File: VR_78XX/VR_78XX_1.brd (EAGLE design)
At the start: 80 x 100 mm, 28 parts, among them U1 7809

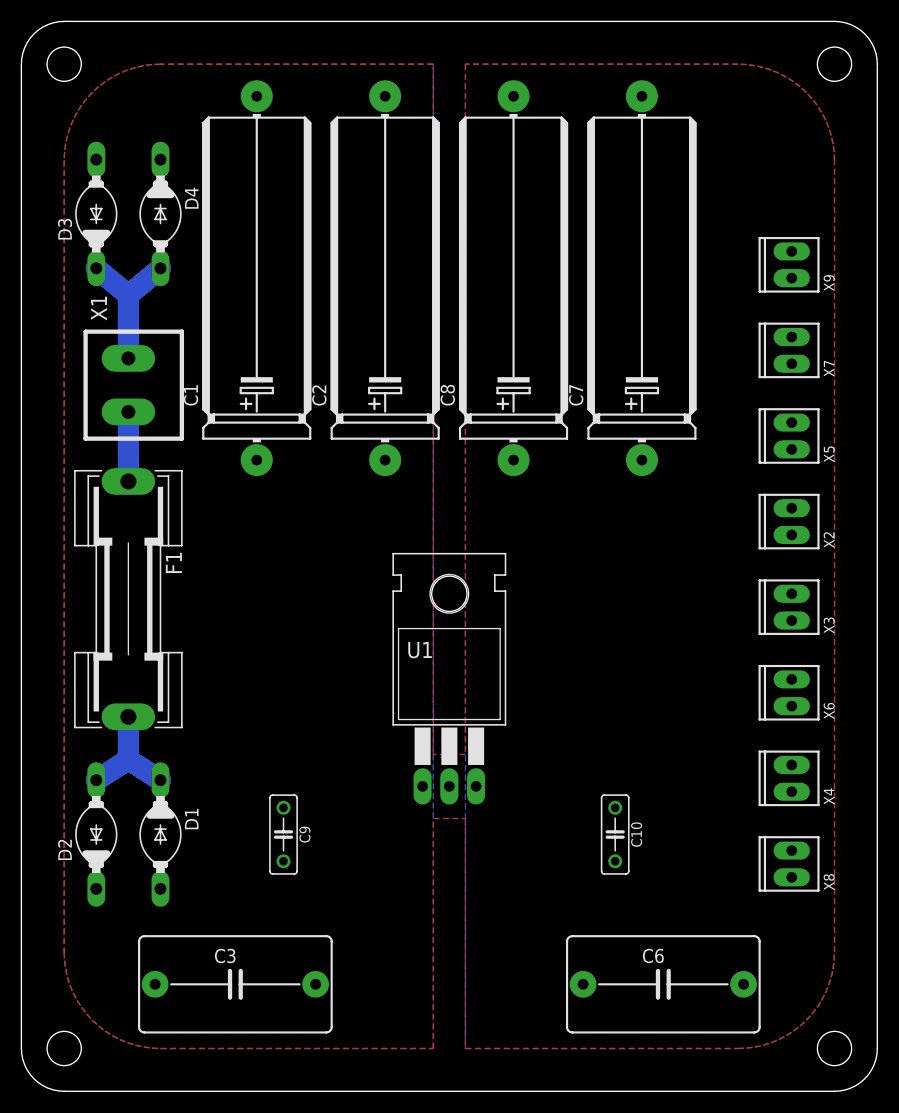
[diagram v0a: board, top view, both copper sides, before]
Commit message: layout, caps
cleaned layout a little bit, added ceramic bypass caps.
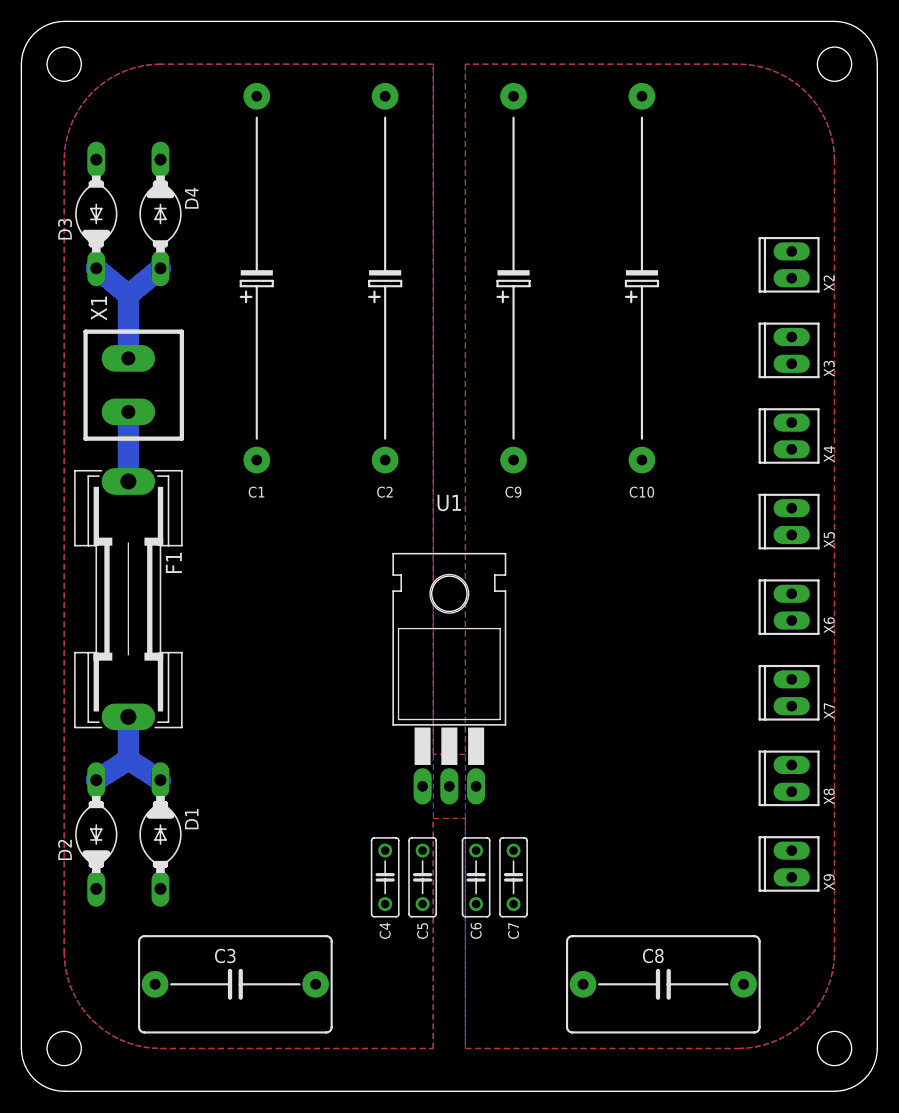
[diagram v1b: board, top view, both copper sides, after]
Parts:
- added C4, C5: 0,1 µF, rcl_a:C050-025X075
- C1, C2: device cap_vishay-pol_a:BC10-30 -> cap_vishay-pol_a:AHT10-30C
- C10, C9: value (none) -> 470 µF; device rcl_a:C050-025X075 -> cap_vishay-pol_a:AHT10-30C
- C6: value 1 µF -> 0,1 µF; device CDE_DMM:1 -> rcl_a:C050-025X075
- C7: value 470 µF -> 0,1 µF; device cap_vishay-pol_a:BC10-30 -> rcl_a:C050-025X075
- C8: value 470 µF -> 1 µF; device cap_vishay-pol_a:BC10-30 -> CDE_DMM:1
- U1: value 7809 -> 78XX
- moved C8 64.5 mm to (121.0, 63.0), turned to 0 degrees
- moved C9 56.3 mm to (107.0, 129.0), turned to 90 degrees
- moved X9 56.0 mm to (133.0, 73.0)
- moved C7 54.3 mm to (107.0, 73.0), turned to 270 degrees
- moved C10 52.1 mm to (119.0, 129.0), turned to 90 degrees
- moved X4 32.0 mm to (133.0, 113.0)
- moved X7 32.0 mm to (133.0, 89.0)
- moved X2 24.0 mm to (133.0, 129.0)
- moved X3 24.0 mm to (133.0, 121.0)
- moved C6 20.2 mm to (103.5, 73.0), turned to 270 degrees
- moved X5 8.00 mm to (133.0, 105.0)
- moved X6 8.00 mm to (133.0, 97.0)
- moved X8 8.00 mm to (133.0, 81.0)
- moved C1 3.00 mm to (83.0, 129.0)
- moved C2 3.00 mm to (95.0, 129.0)
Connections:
- net +5V: now also C10.+, C7.1, C8.1, C9.+; no longer C10.1, C7.+, C8.+
- net GND: now also C10.-, C4.2, C5.2, C7.2, C8.2, C9.-; no longer C10.2, C7.-, C8.-, C9.2
- net VDD2: now also C4.1, C5.1; no longer C9.1
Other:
- board text added: "OUTPUT"

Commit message: added more decoupling caps
Added more decoupling caps
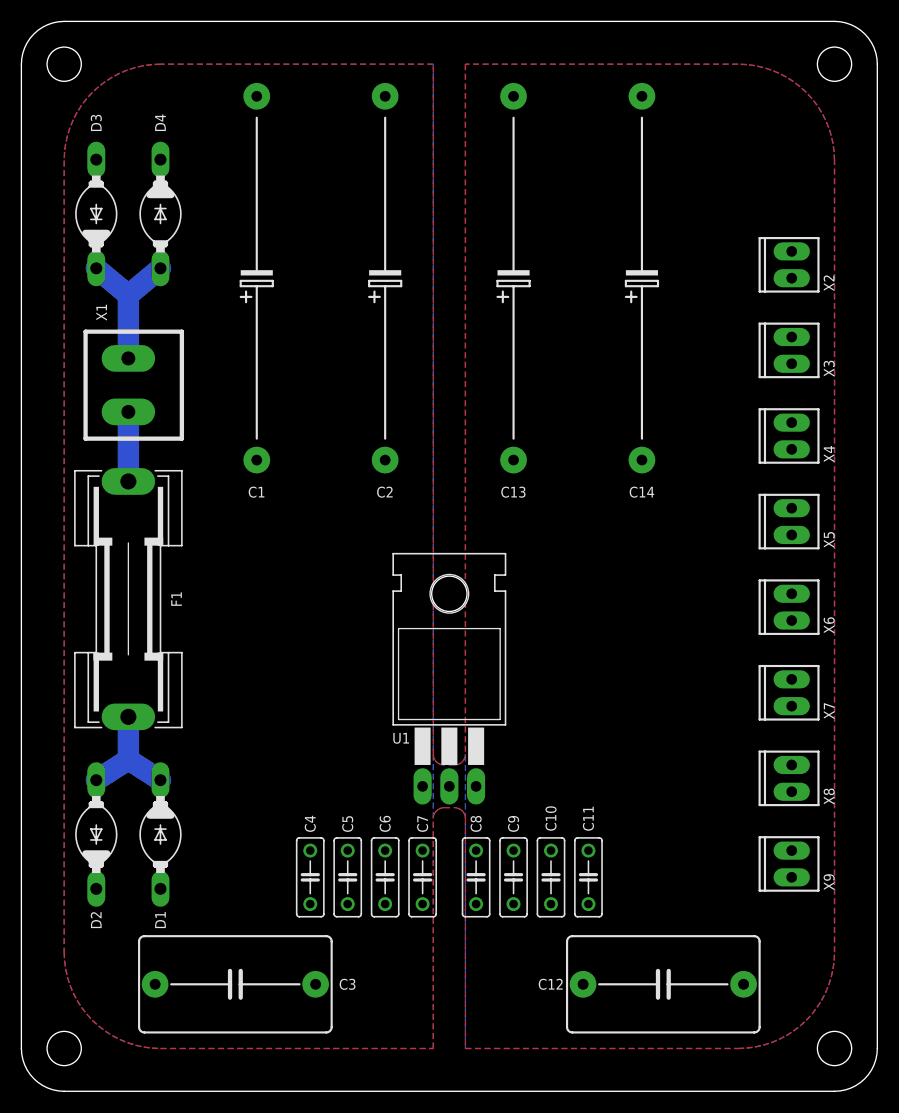
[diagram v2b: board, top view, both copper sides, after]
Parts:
- added C11: 1 µF, rcl_a:C050-025X075
- added C12: 1 µF, CDE_DMM:1
- added C13, C14: 470 µF, cap_vishay-pol_a:AHT10-30C
- C10: value 470 µF -> 1 µF; device cap_vishay-pol_a:AHT10-30C -> rcl_a:C050-025X075
- C4, C5: value 0,1 µF -> 1 µF
- C8: value 1 µF -> 0,1 µF; device CDE_DMM:1 -> rcl_a:C050-025X075
- C9: value 470 µF -> 0,1 µF; device cap_vishay-pol_a:AHT10-30C -> rcl_a:C050-025X075
- moved C10 56.6 mm to (110.5, 73.0), turned to 270 degrees
- moved C9 56.0 mm to (107.0, 73.0)
- moved C8 20.2 mm to (103.5, 73.0), turned to 270 degrees
- moved C6 8.50 mm to (95.0, 73.0), turned to 90 degrees
- moved C7 8.50 mm to (98.5, 73.0)
- moved C4 7.00 mm to (88.0, 73.0), turned to 90 degrees
- moved C5 7.00 mm to (91.5, 73.0)
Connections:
- removed net +5V: C10.+, C6.1, C7.1, C8.1, C9.+, U1.3, X2.1, X3.1, X4.1, X5.1, X6.1, X7.1, X8.1, X9.1
- removed net VDD2: C1.+, C2.+, C3.1, C4.1, C5.1, D2.C, D4.C, U1.1
- new net VIN+: C1.+, C2.+, C3.1, C4.1, C5.1, C6.1, C7.1, D2.C, D4.C, U1.1
- new net VOUT+: C10.1, C11.1, C12.1, C13.+, C14.+, C8.1, C9.1, U1.3, X2.1, X3.1, X4.1, X5.1, X6.1, X7.1, X8.1, X9.1
- net GND: now also C10.2, C11.2, C12.2, C13.-, C14.-, C9.2; no longer C10.-, C9.-
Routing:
- added copper zone on layer 16, net VIN+
- added copper zone on layer 16, net VOUT+
- removed copper zone on layer 16, net +5V
- removed copper zone on layer 16, net VDD2
